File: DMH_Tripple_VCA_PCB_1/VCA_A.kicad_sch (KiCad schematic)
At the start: 19 parts, among them Q1 BC548, Q2 BC548, U1 TL074

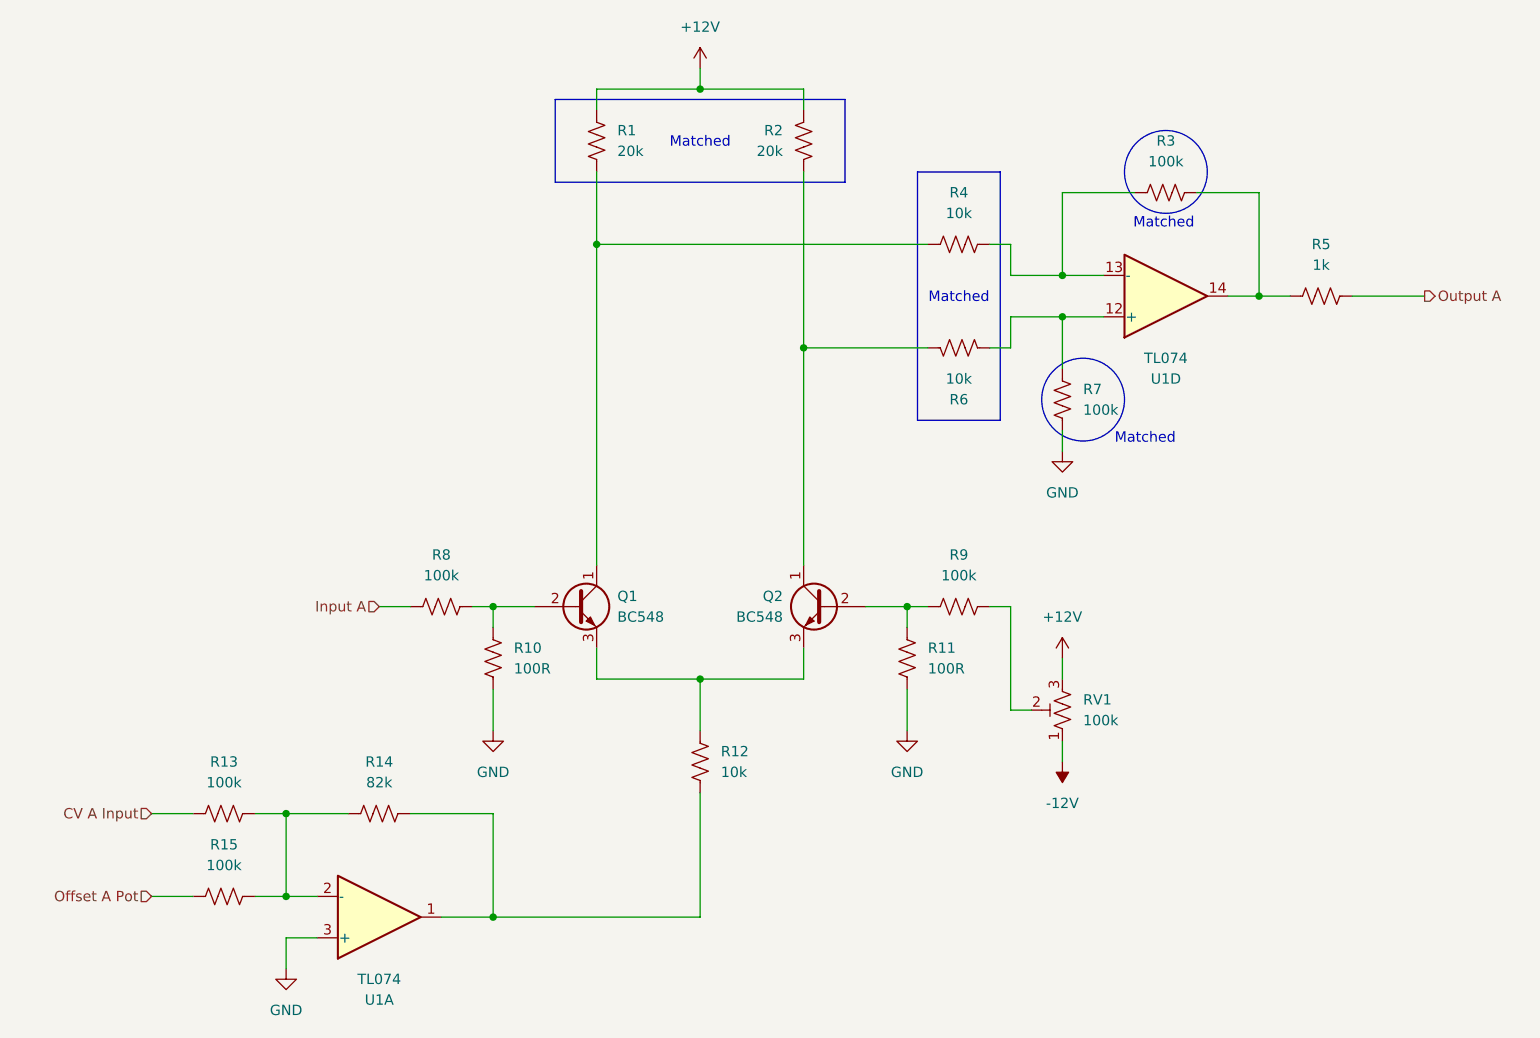
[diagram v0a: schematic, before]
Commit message: PCB 1 component positioning in progress
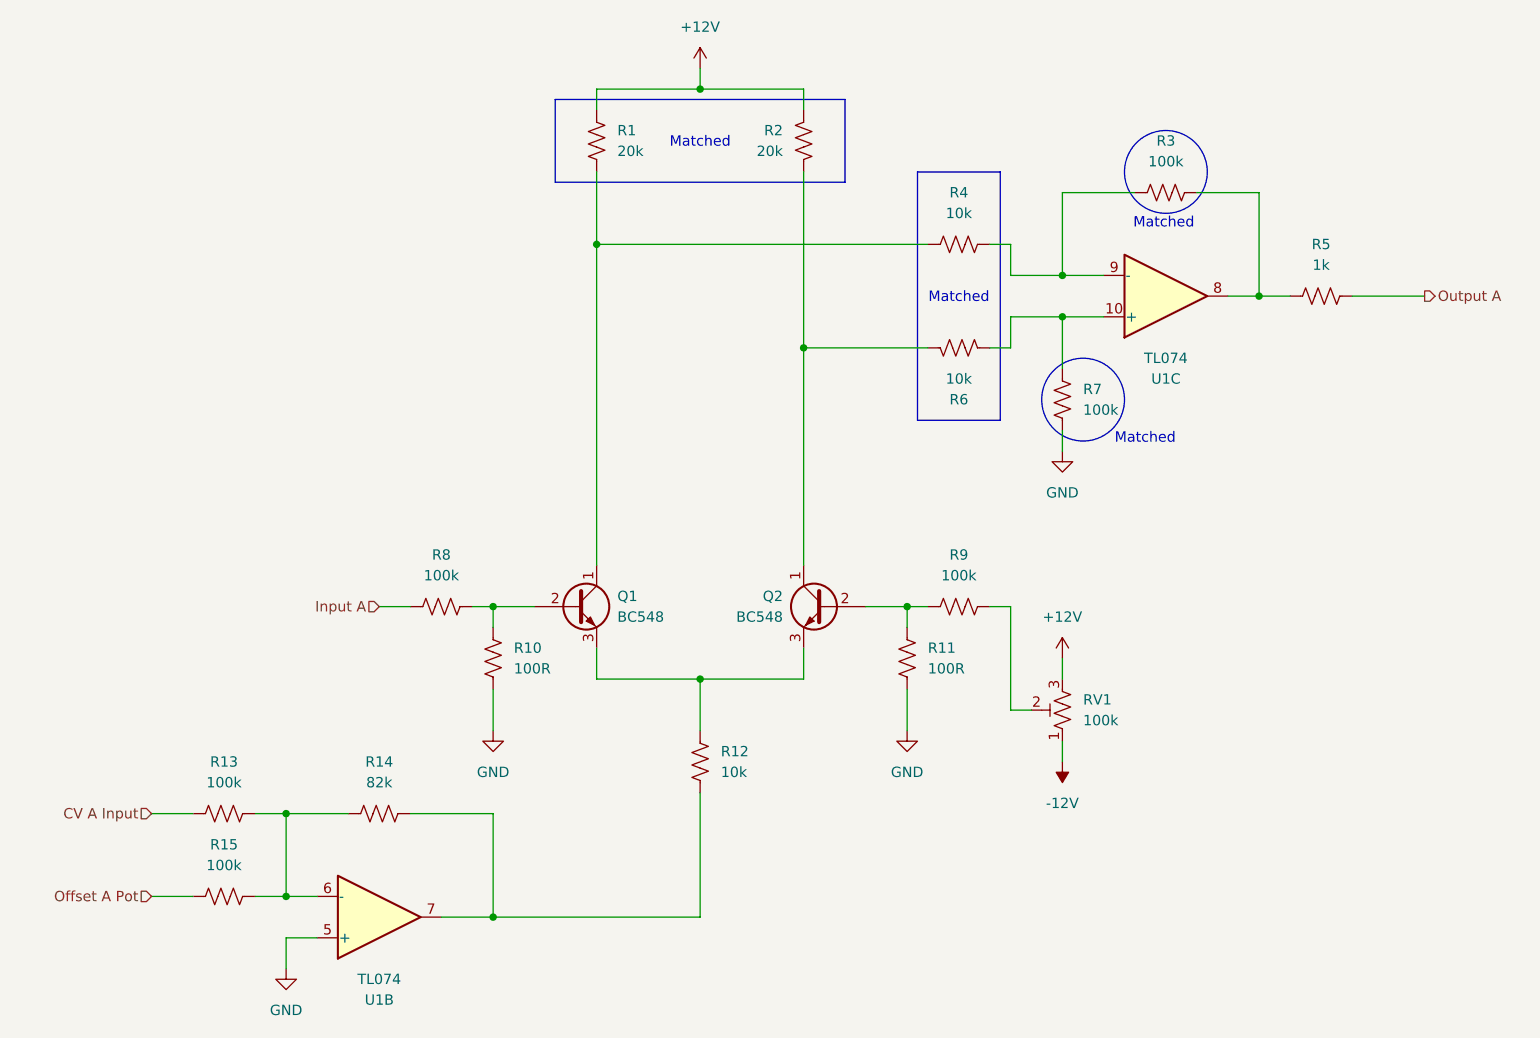
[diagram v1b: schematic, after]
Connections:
- net GND: now also U1.5 (+); no longer U1.3 (+)
- net at R3.1, R5.2: now also U1.8; no longer U1.14
- net at R3.2, R4.1: now also U1.9 (-); no longer U1.13 (-)
- net at R6.1, R7.1: now also U1.10 (+); no longer U1.12 (+)
- net at R12.1, R14.2: now also U1.7; no longer U1.1
- net at R13.2, R14.1, R15.2: now also U1.6 (-); no longer U1.2 (-)
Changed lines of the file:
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@@
 		(at 184.15 76.2 0)
 		(mirror x)
-		(unit 4)
+		(unit 3)
 		(exclude_from_sim no)
 		(in_bom yes)
@@
 				(path "/58f4306d-5387-4983-bb08-41a2313fd315/7ad2d702-dfb7-4d49-a82d-34430dd5948f"
 					(reference "U1")
-					(unit 4)
+					(unit 3)
 				)
 			)
@@
 		(at 87.63 152.4 0)
 		(mirror x)
-		(unit 1)
+		(unit 2)
 		(exclude_from_sim no)
 		(in_bom yes)
@@
 				(path "/58f4306d-5387-4983-bb08-41a2313fd315/7ad2d702-dfb7-4d49-a82d-34430dd5948f"
 					(reference "U1")
-					(unit 1)
+					(unit 2)
 				)
 			)

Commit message: Adjusted OpAmp pinouts for placement
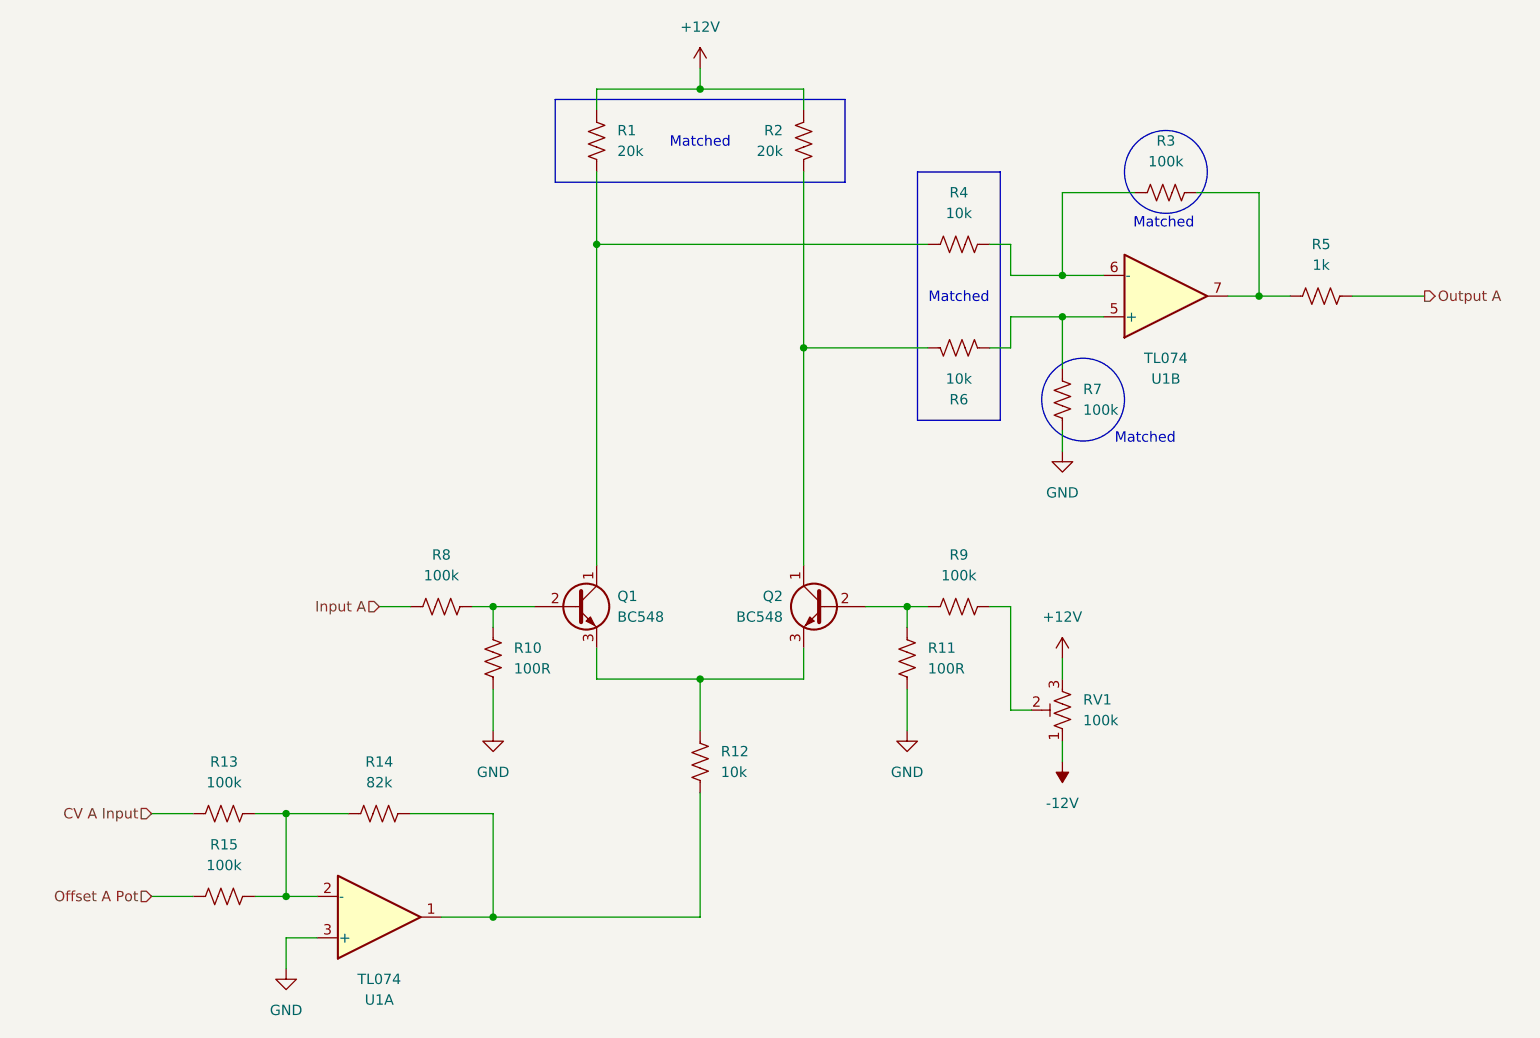
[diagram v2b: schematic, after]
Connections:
- net GND: now also U1.3 (+); no longer U1.5 (+)
- net at R3.1, R5.2: now also U1.7; no longer U1.8
- net at R3.2, R4.1: now also U1.6 (-); no longer U1.9 (-)
- net at R6.1, R7.1: now also U1.5 (+); no longer U1.10 (+)
- net at R13.2, R14.1, R15.2: now also U1.2 (-); no longer U1.6 (-)
- net at R12.1, R14.2: now also U1.1; no longer U1.7
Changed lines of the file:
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@@
 		(at 184.15 76.2 0)
 		(mirror x)
-		(unit 3)
+		(unit 2)
 		(exclude_from_sim no)
 		(in_bom yes)
@@
 				(path "/58f4306d-5387-4983-bb08-41a2313fd315/7ad2d702-dfb7-4d49-a82d-34430dd5948f"
 					(reference "U1")
-					(unit 3)
+					(unit 2)
 				)
 			)
@@
 		(at 87.63 152.4 0)
 		(mirror x)
-		(unit 2)
+		(unit 1)
 		(exclude_from_sim no)
 		(in_bom yes)
@@
 				(path "/58f4306d-5387-4983-bb08-41a2313fd315/7ad2d702-dfb7-4d49-a82d-34430dd5948f"
 					(reference "U1")
-					(unit 2)
+					(unit 1)
 				)
 			)

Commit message: Started routing over with upright resistor fps
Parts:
- R1, R10, R11, R12, R13, R14, R15, R2, R3, R4, R5, R6, R7, R8, R9: footprint Resistor_THT:R_Axial_DIN0207_L6.3mm_D2.5mm_P7.62mm_Horizontal -> Resistor_THT:R_Axial_DIN0207_L6.3mm_D2.5mm_P2.54mm_Vertical
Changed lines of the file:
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@@
 			)
 		)
-		(property "Footprint" "Resistor_THT:R_Axial_DIN0207_L6.3mm_D2.5mm_P7.62mm_Horizontal"
+		(property "Footprint" "Resistor_THT:R_Axial_DIN0207_L6.3mm_D2.5mm_P2.54mm_Vertical"
 			(at 183.896 64.516 90)
 			(effects
@@
 			)
 		)
-		(property "Footprint" "Resistor_THT:R_Axial_DIN0207_L6.3mm_D2.5mm_P7.62mm_Horizontal"
+		(property "Footprint" "Resistor_THT:R_Axial_DIN0207_L6.3mm_D2.5mm_P2.54mm_Vertical"
 			(at 151.384 120.396 90)
 			(effects
@@
 			)
 		)
-		(property "Footprint" "Resistor_THT:R_Axial_DIN0207_L6.3mm_D2.5mm_P7.62mm_Horizontal"
+		(property "Footprint" "Resistor_THT:R_Axial_DIN0207_L6.3mm_D2.5mm_P2.54mm_Vertical"
 			(at 202.946 77.216 90)
 			(effects
@@
 			)
 		)
-		(property "Footprint" "Resistor_THT:R_Axial_DIN0207_L6.3mm_D2.5mm_P7.62mm_Horizontal"
+		(property "Footprint" "Resistor_THT:R_Axial_DIN0207_L6.3mm_D2.5mm_P2.54mm_Vertical"
 			(at 100.584 120.396 90)
 			(effects
@@
 			)
 		)
-		(property "Footprint" "Resistor_THT:R_Axial_DIN0207_L6.3mm_D2.5mm_P7.62mm_Horizontal"
+		(property "Footprint" "Resistor_THT:R_Axial_DIN0207_L6.3mm_D2.5mm_P2.54mm_Vertical"
 			(at 158.496 81.534 90)
 			(effects
@@
 			)
 		)
-		(property "Footprint" "Resistor_THT:R_Axial_DIN0207_L6.3mm_D2.5mm_P7.62mm_Horizontal"
+		(property "Footprint" "Resistor_THT:R_Axial_DIN0207_L6.3mm_D2.5mm_P2.54mm_Vertical"
 			(at 94.996 115.316 90)
 			(effects
@@
 			)
 		)
-		(property "Footprint" "Resistor_THT:R_Axial_DIN0207_L6.3mm_D2.5mm_P7.62mm_Horizontal"
+		(property "Footprint" "Resistor_THT:R_Axial_DIN0207_L6.3mm_D2.5mm_P2.54mm_Vertical"
 			(at 113.284 56.896 90)
 			(effects
@@
 			)
 		)
-		(property "Footprint" "Resistor_THT:R_Axial_DIN0207_L6.3mm_D2.5mm_P7.62mm_Horizontal"
+		(property "Footprint" "Resistor_THT:R_Axial_DIN0207_L6.3mm_D2.5mm_P2.54mm_Vertical"
 			(at 158.496 115.316 90)
 			(effects
@@
 			)
 		)
-		(property "Footprint" "Resistor_THT:R_Axial_DIN0207_L6.3mm_D2.5mm_P7.62mm_Horizontal"
+		(property "Footprint" "Resistor_THT:R_Axial_DIN0207_L6.3mm_D2.5mm_P2.54mm_Vertical"
 			(at 158.496 70.866 90)
 			(effects
@@
 			)
 		)
-		(property "Footprint" "Resistor_THT:R_Axial_DIN0207_L6.3mm_D2.5mm_P7.62mm_Horizontal"
+		(property "Footprint" "Resistor_THT:R_Axial_DIN0207_L6.3mm_D2.5mm_P2.54mm_Vertical"
 			(at 87.884 138.684 90)
 			(effects
@@
 			)
 		)
-		(property "Footprint" "Resistor_THT:R_Axial_DIN0207_L6.3mm_D2.5mm_P7.62mm_Horizontal"
+		(property "Footprint" "Resistor_THT:R_Axial_DIN0207_L6.3mm_D2.5mm_P2.54mm_Vertical"
 			(at 172.466 89.154 90)
 			(effects
@@
 			)
 		)
-		(property "Footprint" "Resistor_THT:R_Axial_DIN0207_L6.3mm_D2.5mm_P7.62mm_Horizontal"
+		(property "Footprint" "Resistor_THT:R_Axial_DIN0207_L6.3mm_D2.5mm_P2.54mm_Vertical"
 			(at 68.834 138.684 90)
 			(effects
@@
 			)
 		)
-		(property "Footprint" "Resistor_THT:R_Axial_DIN0207_L6.3mm_D2.5mm_P7.62mm_Horizontal"
+		(property "Footprint" "Resistor_THT:R_Axial_DIN0207_L6.3mm_D2.5mm_P2.54mm_Vertical"
 			(at 68.834 148.844 90)
 			(effects
@@
 			)
 		)
-		(property "Footprint" "Resistor_THT:R_Axial_DIN0207_L6.3mm_D2.5mm_P7.62mm_Horizontal"
+		(property "Footprint" "Resistor_THT:R_Axial_DIN0207_L6.3mm_D2.5mm_P2.54mm_Vertical"
 			(at 140.716 56.896 90)
 			(effects
@@
 			)
 		)
-		(property "Footprint" "Resistor_THT:R_Axial_DIN0207_L6.3mm_D2.5mm_P7.62mm_Horizontal"
+		(property "Footprint" "Resistor_THT:R_Axial_DIN0207_L6.3mm_D2.5mm_P2.54mm_Vertical"
 			(at 125.984 133.096 90)
 			(effects

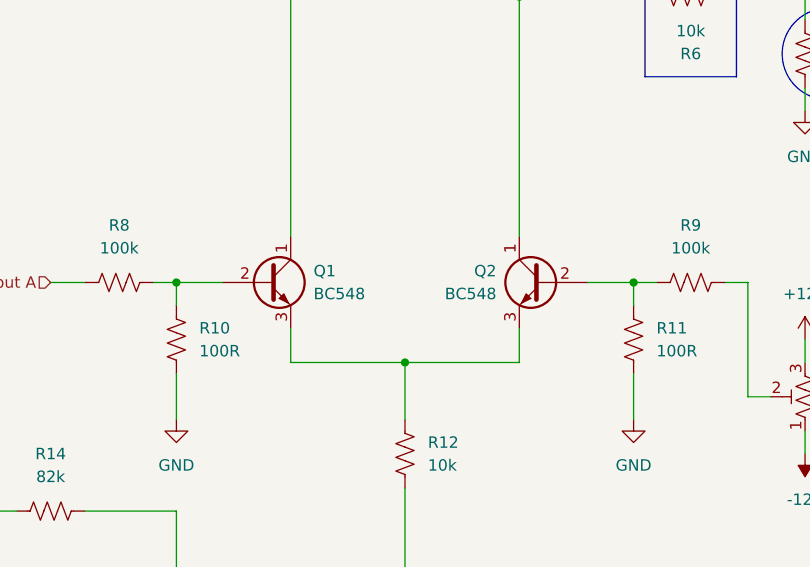
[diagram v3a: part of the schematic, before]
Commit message: Converted PCB 1 project to KiCad 9
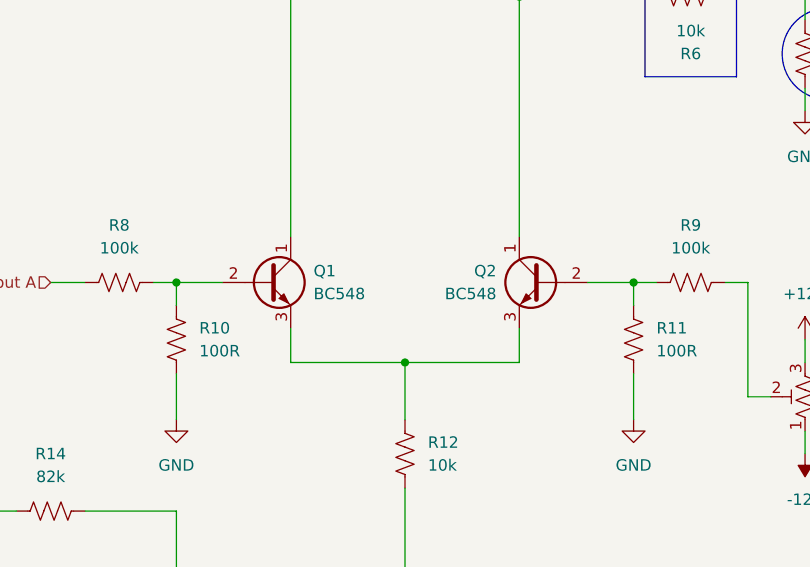
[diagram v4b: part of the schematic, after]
